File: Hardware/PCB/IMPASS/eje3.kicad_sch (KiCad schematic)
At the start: 8 parts, among them Q17 DMN3008SFG, Q18 DMN3008SFG, Q19 DMN3008SFG, Q20 DMN3008SFG, Q21 DMN3008SFG, Q22 DMN3008SFG, Q23 DMN3008SFG, Q24 DMN3008SFG

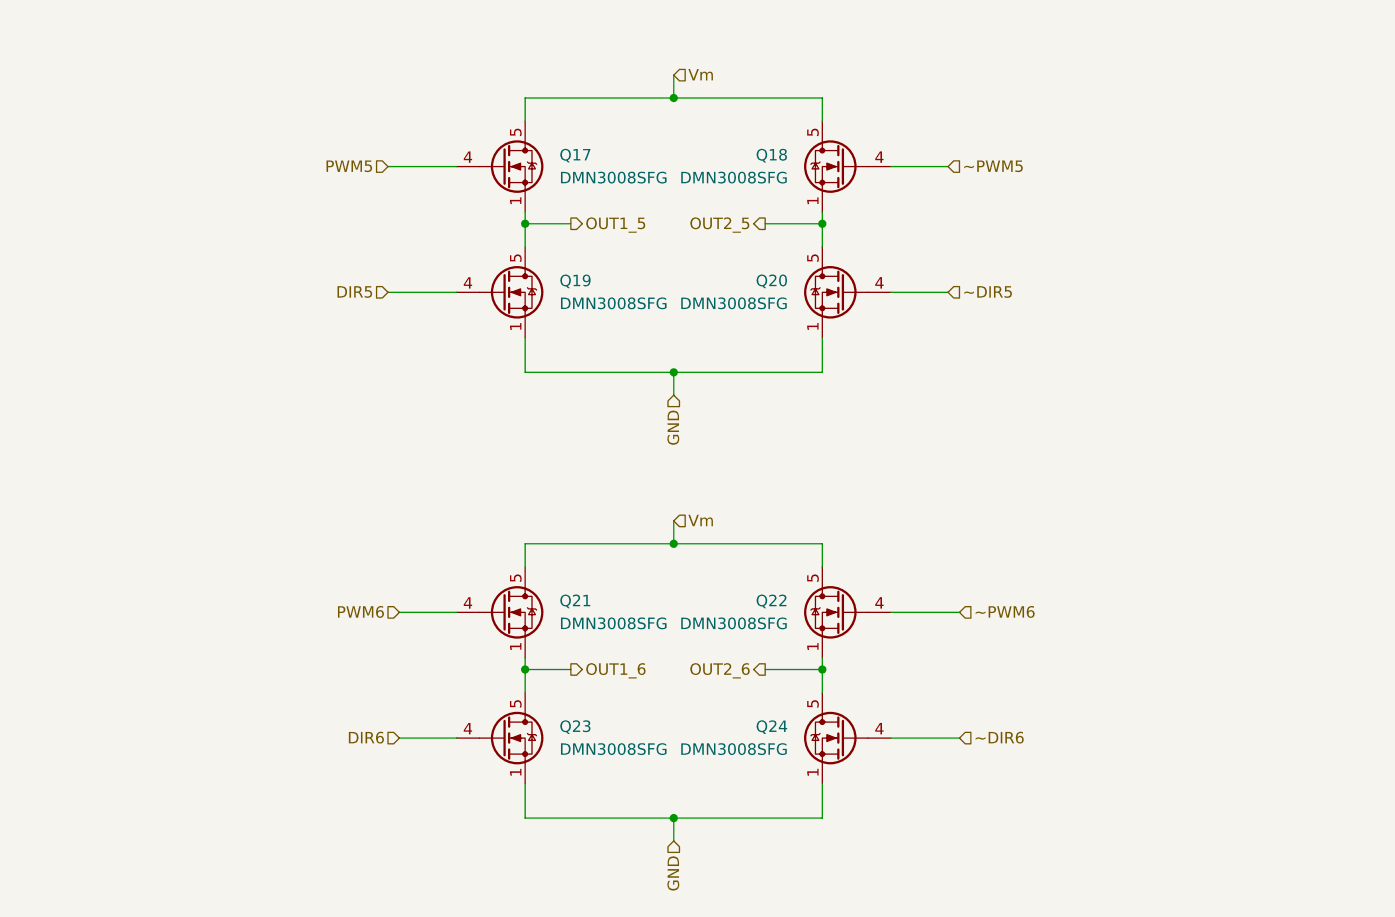
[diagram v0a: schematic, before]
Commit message: Restore all the schematics
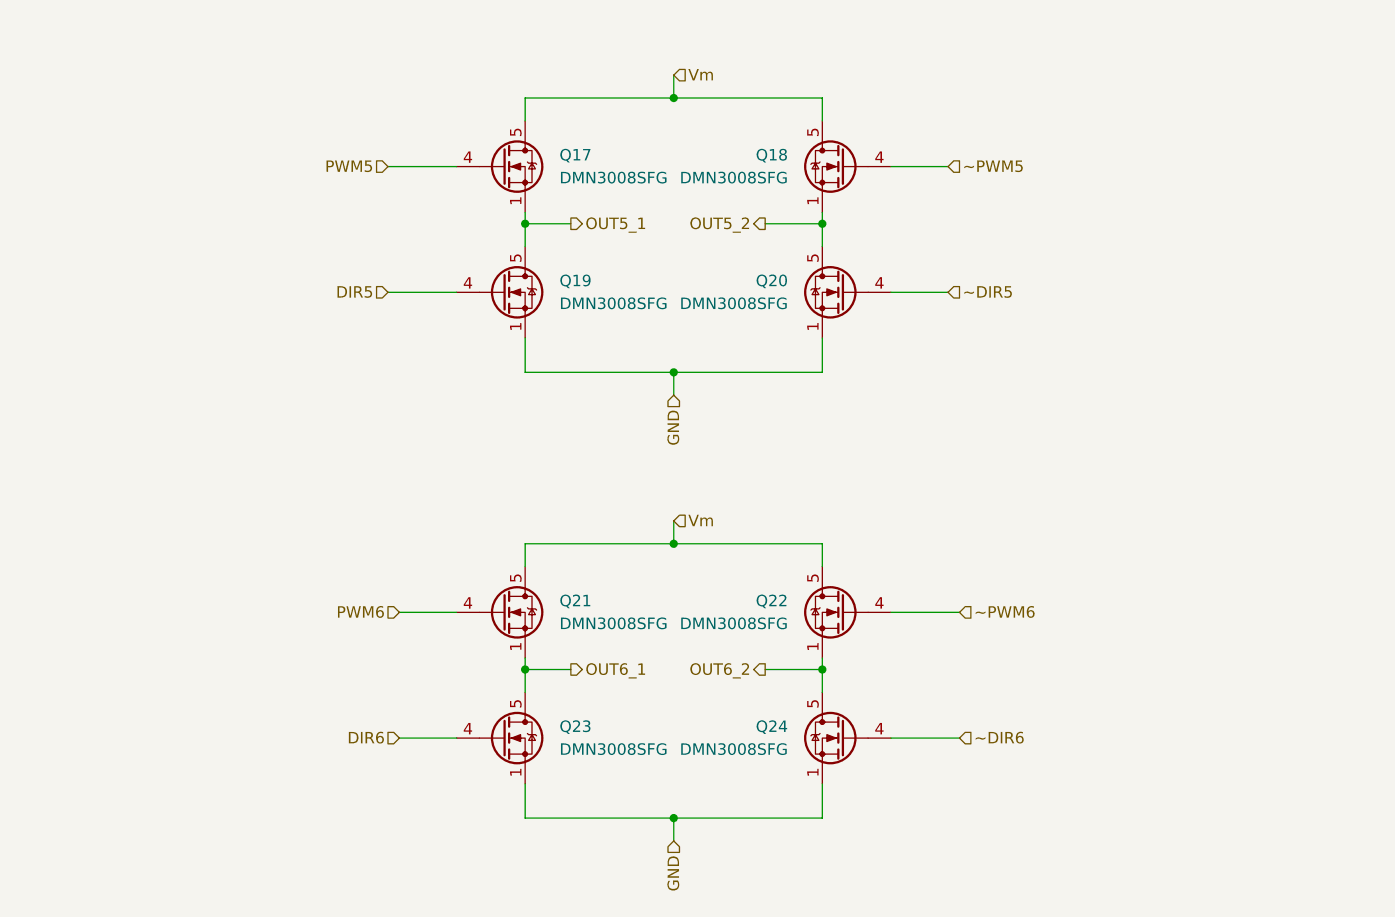
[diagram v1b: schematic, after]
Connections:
- net OUT1_5 renamed OUT5_1
- net OUT1_6 renamed OUT6_1
- net OUT2_5 renamed OUT5_2
- net OUT2_6 renamed OUT6_2
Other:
- company: (none) -> Luis Miguel Carmona Cortés
- title: (none) -> IMPASS 
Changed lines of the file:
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@@
 (kicad_sch
-	(version 20231120)
+	(version 20250114)
 	(generator "eeschema")
-	(generator_version "8.0")
+	(generator_version "9.0")
 	(paper "A4")
+	(title_block
+		(title "IMPASS ")
+		(date "2026-01-31")
+		(rev "v2.0")
+		(company "Luis Miguel Carmona Cortés")
+		(comment 1 "Puentes H del eje3")
+	)
 	(junction
 		(at 106.68 111.76)
@@
 		)
 	)
-	(hierarchical_label "OUT1_5"
+	(hierarchical_label "OUT5_1"
 		(shape output)
 		(at 111.76 62.23 0)
@@
 		)
 	)
-	(hierarchical_label "OUT1_6"
+	(hierarchical_label "OUT6_1"
 		(shape output)
 		(at 111.76 111.76 0)
@@
 		)
 	)
-	(hierarchical_label "OUT2_5"
+	(hierarchical_label "OUT5_2"
 		(shape output)
 		(at 133.35 62.23 180)
@@
 		)
 	)
-	(hierarchical_label "OUT2_6"
+	(hierarchical_label "OUT6_2"
 		(shape output)
 		(at 133.35 111.76 180)
@@
 		(instances
 			(project "IMPASS"
-				(path "/731b3037-3e9a-4423-b2c0-b5bf223d88c2/f88d884c-2e90-4ed2-b40a-13211fa440f1/e6bf87d9-9b17-4c78-8408-bae94d45215c"
+				(path "/731b3037-3e9a-4423-b2c0-b5bf223d88c2/acd98061-6367-4cb8-aa42-1ec0ef88ad06/46ad667e-284c-4a90-8298-bcdd50eeeed0"
 					(reference "Q20")
 					(unit 1)
@@
 		(instances
 			(project "IMPASS"
-				(path "/731b3037-3e9a-4423-b2c0-b5bf223d88c2/f88d884c-2e90-4ed2-b40a-13211fa440f1/e6bf87d9-9b17-4c78-8408-bae94d45215c"
+				(path "/731b3037-3e9a-4423-b2c0-b5bf223d88c2/acd98061-6367-4cb8-aa42-1ec0ef88ad06/46ad667e-284c-4a90-8298-bcdd50eeeed0"
 					(reference "Q19")
 					(unit 1)
@@
 		(instances
 			(project "IMPASS"
-				(path "/731b3037-3e9a-4423-b2c0-b5bf223d88c2/f88d884c-2e90-4ed2-b40a-13211fa440f1/e6bf87d9-9b17-4c78-8408-bae94d45215c"
+				(path "/731b3037-3e9a-4423-b2c0-b5bf223d88c2/acd98061-6367-4cb8-aa42-1ec0ef88ad06/46ad667e-284c-4a90-8298-bcdd50eeeed0"
 					(reference "Q17")
 					(unit 1)
@@
 		(instances
 			(project "IMPASS"
-				(path "/731b3037-3e9a-4423-b2c0-b5bf223d88c2/f88d884c-2e90-4ed2-b40a-13211fa440f1/e6bf87d9-9b17-4c78-8408-bae94d45215c"
+				(path "/731b3037-3e9a-4423-b2c0-b5bf223d88c2/acd98061-6367-4cb8-aa42-1ec0ef88ad06/46ad667e-284c-4a90-8298-bcdd50eeeed0"
 					(reference "Q21")
 					(unit 1)
@@
 		(instances
 			(project "IMPASS"
-				(path "/731b3037-3e9a-4423-b2c0-b5bf223d88c2/f88d884c-2e90-4ed2-b40a-13211fa440f1/e6bf87d9-9b17-4c78-8408-bae94d45215c"
+				(path "/731b3037-3e9a-4423-b2c0-b5bf223d88c2/acd98061-6367-4cb8-aa42-1ec0ef88ad06/46ad667e-284c-4a90-8298-bcdd50eeeed0"
 					(reference "Q18")
 					(unit 1)
@@
 		(instances
 			(project "IMPASS"
-				(path "/731b3037-3e9a-4423-b2c0-b5bf223d88c2/f88d884c-2e90-4ed2-b40a-13211fa440f1/e6bf87d9-9b17-4c78-8408-bae94d45215c"
+				(path "/731b3037-3e9a-4423-b2c0-b5bf223d88c2/acd98061-6367-4cb8-aa42-1ec0ef88ad06/46ad667e-284c-4a90-8298-bcdd50eeeed0"
 					(reference "Q22")
 					(unit 1)
@@
 		(instances
 			(project "IMPASS"
-				(path "/731b3037-3e9a-4423-b2c0-b5bf223d88c2/f88d884c-2e90-4ed2-b40a-13211fa440f1/e6bf87d9-9b17-4c78-8408-bae94d45215c"
+				(path "/731b3037-3e9a-4423-b2c0-b5bf223d88c2/acd98061-6367-4cb8-aa42-1ec0ef88ad06/46ad667e-284c-4a90-8298-bcdd50eeeed0"
 					(reference "Q23")
 					(unit 1)
@@
 		(instances
 			(project "IMPASS"
-				(path "/731b3037-3e9a-4423-b2c0-b5bf223d88c2/f88d884c-2e90-4ed2-b40a-13211fa440f1/e6bf87d9-9b17-4c78-8408-bae94d45215c"
+				(path "/731b3037-3e9a-4423-b2c0-b5bf223d88c2/acd98061-6367-4cb8-aa42-1ec0ef88ad06/46ad667e-284c-4a90-8298-bcdd50eeeed0"
 					(reference "Q24")
 					(unit 1)

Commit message: Hardware: update schematic and PCB layout
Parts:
- removed Q17, Q18, Q21, Q22: DMN3008SFG, Package_SON:Diodes_PowerDI3333-8, symbol Transistor_FET:DMN3008SFG
- added Q17, Q22: BC847BDW1, Package_TO_SOT_SMD:SOT-363_SC-70-6, symbol Transistor_BJT:BC847BDW1
- added Q18, Q21, Q25, Q26: DMP3013SFV, Package_SON:Diodes_PowerDI3333-8, symbol Transistor_FET:DMP3013SFV
- added R75, R76, R77, R78, R79, R80, R81, R82: 10k, Resistor_SMD:R_0603_1608Metric, symbol Device:R
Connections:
- net GND: now also Q17.1 (E1), Q17.4 (E2), Q22.1 (E1), Q22.4 (E2)
- net OUT5_1: now also Q18.5 (D)
- net OUT5_2: now also Q21.5 (D)
- net OUT6_1: now also Q25.5 (D)
- net OUT6_2: now also Q26.5 (D)
- net PWM5: now also R75.1
- net PWM6: now also R79.1
- net Vm: now also Q18.1 (S), Q18.2 (S), Q18.3 (S), Q21.1 (S), Q21.2 (S), Q21.3 (S), Q25.1 (S), Q25.2 (S), Q25.3 (S), Q26.1 (S), Q26.2 (S), Q26.3 (S), R76.1, R77.1, R80.1, R81.1
- net ~PWM5: now also R78.2
- net ~PWM6: now also R82.2
- new net: Q22.6 (C1), Q25.4 (G), R80.2
- new net: Q22.5 (B2), R82.1
- new net: Q22.2 (B1), R79.2
- new net: Q17.6 (C1), Q18.4 (G), R76.2
- new net: Q17.5 (B2), R78.1
- new net: Q17.3 (C2), Q21.4 (G), R77.2
- new net: Q17.2 (B1), R75.2
- new net: Q22.3 (C2), Q26.4 (G), R81.2
